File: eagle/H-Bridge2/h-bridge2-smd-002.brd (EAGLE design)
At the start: 100 x 80 mm, 29 parts

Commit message: eagle merge template board with h-br
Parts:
- RLA: device rcl:0411/15 -> rcl:R0603
- moved C4 100.6 mm to (69.8, 14.0)
- moved RLA 95.3 mm to (57.1, 15.2)
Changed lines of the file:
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@@
 </element>
 <element name="C1" library="rcl" package="C025-025X050" value="" x="55.88" y="-86.36"/>
-<element name="C4" library="rcl" package="C025-025X050" value="" x="62.23" y="-86.36"/>
+<element name="C4" library="rcl" package="C025-025X050" value="" x="69.85" y="13.97"/>
 <element name="RHA" library="rcl" package="0411/15" value="" x="20.32" y="-80.01"/>
-<element name="RLA" library="rcl" package="0411/15" value="" x="55.88" y="-80.01"/>
+<element name="RLA" library="rcl" package="R0603" value="" x="57.15" y="15.24"/>
 <element name="RHB" library="rcl" package="0411/15" value="" x="38.1" y="-80.01"/>
 <element name="RLB" library="rcl" package="0411/15" value="" x="7.62" y="-86.36"/>
@@
 <contactref element="RLA" pad="2"/>
 <contactref element="LA" pad="G"/>
-<wire x1="63.5" y1="-80.01" x2="1.27" y2="-49.53" width="0" layer="19" extent="1-1"/>
+<wire x1="58" y1="15.24" x2="1.27" y2="-49.53" width="0" layer="19" extent="1-1"/>
 </signal>
 <signal name="N$6">
@@
 <contactref element="UA" pad="1"/>
 <contactref element="RLA" pad="1"/>
-<wire x1="0" y1="-6.35" x2="48.26" y2="-80.01" width="0" layer="19" extent="1-1"/>
+<wire x1="0" y1="-6.35" x2="56.3" y2="15.24" width="0" layer="19" extent="1-1"/>
 </signal>
 <signal name="N$11">
@@
 <wire x1="39.37" y1="-86.36" x2="21.59" y2="-72.39" width="0" layer="19" extent="1-1"/>
 <wire x1="16.51" y1="-49.53" x2="21.59" y2="-72.39" width="0" layer="19" extent="1-1"/>
-<wire x1="63.5" y1="-86.36" x2="39.37" y2="-86.36" width="0" layer="19" extent="1-1"/>
-<wire x1="53.34" y1="-57.15" x2="63.5" y2="-86.36" width="0" layer="19" extent="1-1"/>
+<wire x1="71.12" y1="13.97" x2="39.37" y2="-86.36" width="0" layer="19" extent="1-1"/>
+<wire x1="53.34" y1="-57.15" x2="71.12" y2="13.97" width="0" layer="19" extent="1-1"/>
 <wire x1="19.05" y1="-16.51" x2="16.51" y2="-49.53" width="0" layer="19" extent="1-1"/>
 <wire x1="57.15" y1="-22.86" x2="53.34" y2="-57.15" width="0" layer="19" extent="1-1"/>
@@
 <contactref element="UB" pad="6"/>
 <contactref element="C4" pad="1"/>
-<wire x1="60.96" y1="-86.36" x2="0" y2="-78.74" width="0" layer="19" extent="1-1"/>
+<wire x1="68.58" y1="13.97" x2="0" y2="-78.74" width="0" layer="19" extent="1-1"/>
 <wire x1="19.05" y1="-19.05" x2="0" y2="-78.74" width="0" layer="19" extent="1-1"/>
 </signal>

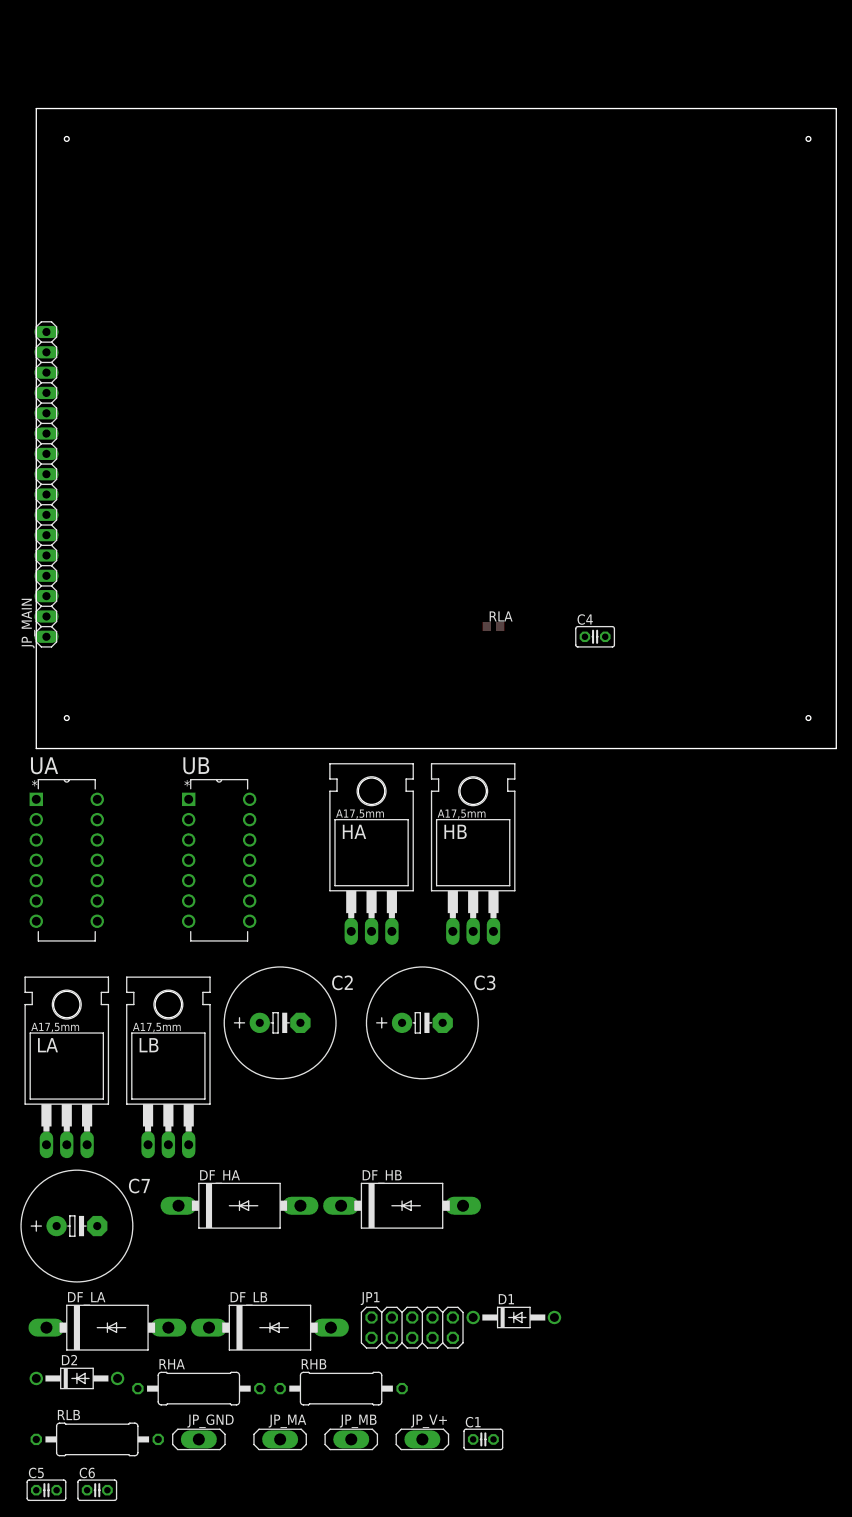
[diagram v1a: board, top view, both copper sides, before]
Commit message: H-bridge on SMD
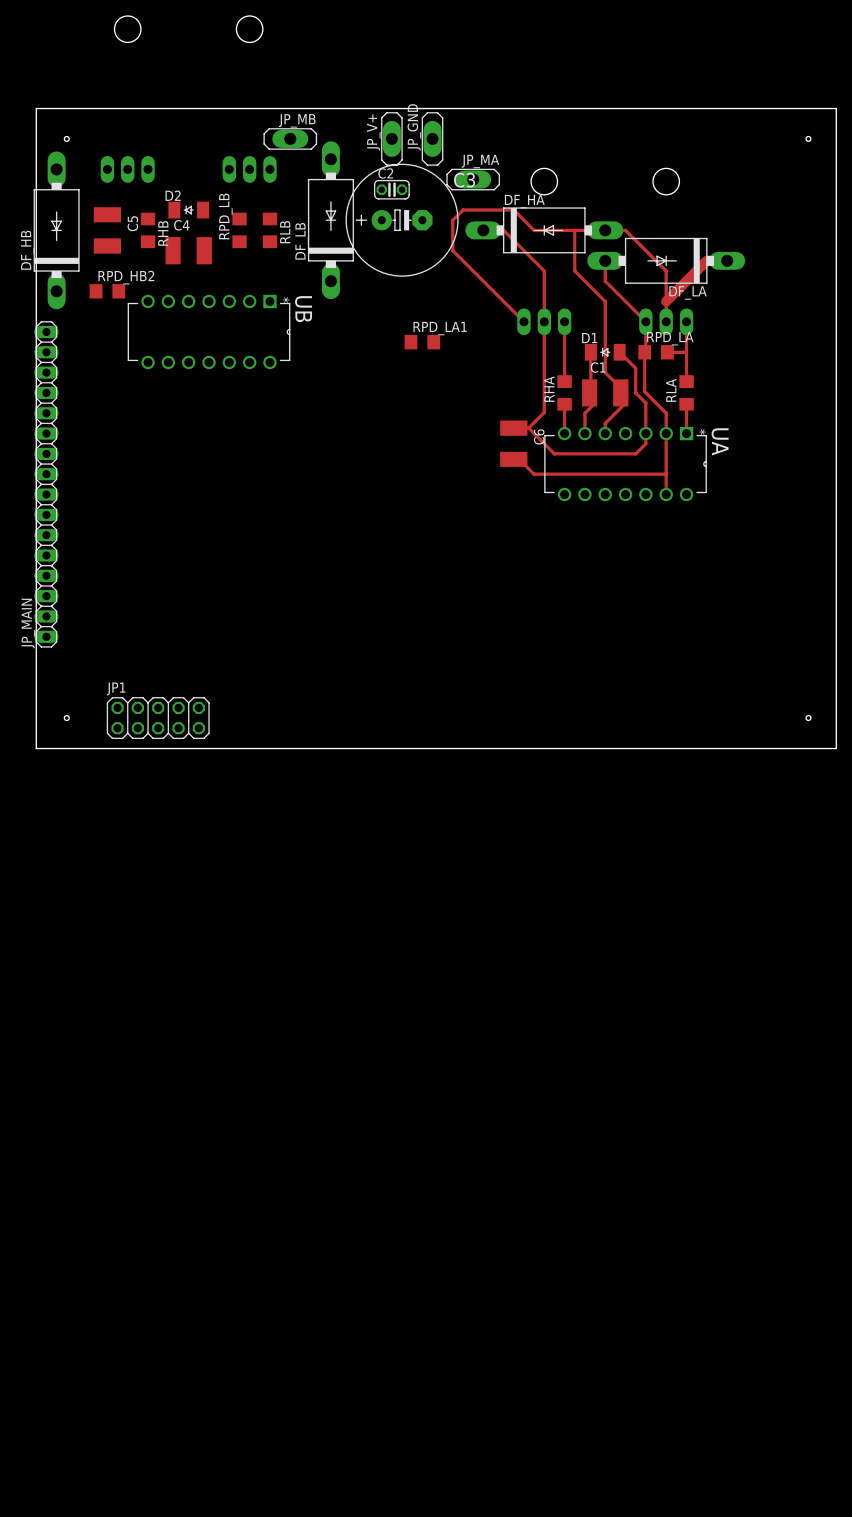
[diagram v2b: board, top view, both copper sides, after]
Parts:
- removed C7: (no value), rcl:E5-13
- added RPD_HB2, RPD_LA, RPD_LA1, RPD_LB: (no value), rcl:R1206
- C1, C4, C5, C6: device rcl:C025-025X050 -> rcl:C4532
- C2: device rcl:E5-13 -> rcl:C025-024X044
- D1, D2: value 1N4004 -> CGRM4001-G; device diode:DO41-10 -> diode:SOD-123_MINI-SMA
- RHA, RHB, RLB: device rcl:0411/15 -> rcl:R1206
- RLA: device rcl:R0603 -> rcl:R1206
- moved JP_GND 165.2 mm to (49.5, 76.2), turned to 90 degrees
- moved JP_MB 162.7 mm to (31.8, 76.2)
- moved JP_V+ 162.6 mm to (44.5, 76.2), turned to 90 degrees
- moved JP_MA 159.3 mm to (54.6, 71.1)
- moved C5 157.7 mm to (8.89, 64.8), turned to 270 degrees
- moved RLB 152.7 mm to (29.2, 64.8), turned to 270 degrees
- moved DF_LA 150.5 mm to (78.7, 61.0), turned to 180 degrees
- moved RHB 146.8 mm to (14.0, 64.8), turned to 270 degrees
- moved D2 146.7 mm to (19.1, 67.3)
- moved C6 140.8 mm to (59.7, 38.1), turned to 270 degrees
- moved DF_LB 138.6 mm to (36.8, 66.0), turned to 90 degrees
- moved RHA 132.6 mm to (66.0, 44.5), turned to 90 degrees
- moved C1 131.7 mm to (71.1, 44.5)
- moved DF_HB 129.3 mm to (2.54, 64.8), turned to 90 degrees
- moved DF_HA 127.7 mm to (63.5, 64.8)
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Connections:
- net N$13: now also C2.1; no longer C2.+, C7.+
- net N$16: now also RPD_HB2.1
- net N$17: now also RPD_LA1.1
- net N$4: now also C2.2, RPD_LA.1, RPD_LB.1; no longer C2.-, C7.-
- net N$5: now also RPD_LA.2
- net N$6: now also RPD_LA1.2
- net N$7: now also RPD_HB2.2
- net N$8: now also RPD_LB.2
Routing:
- net N$17: track 0.00 -> 92.7 mm
- net N$13: track 0.00 -> 61.3 mm
- net N$4: track 0.00 -> 52.3 mm
- net N$14: track 0.00 -> 11.0 mm
- net N$5: track 0.00 -> 9.86 mm
- net N$6: track 0.00 -> 7.47 mm
- net N$9: track 0.00 -> 3.66 mm
- net N$10: track 0.00 -> 3.66 mm

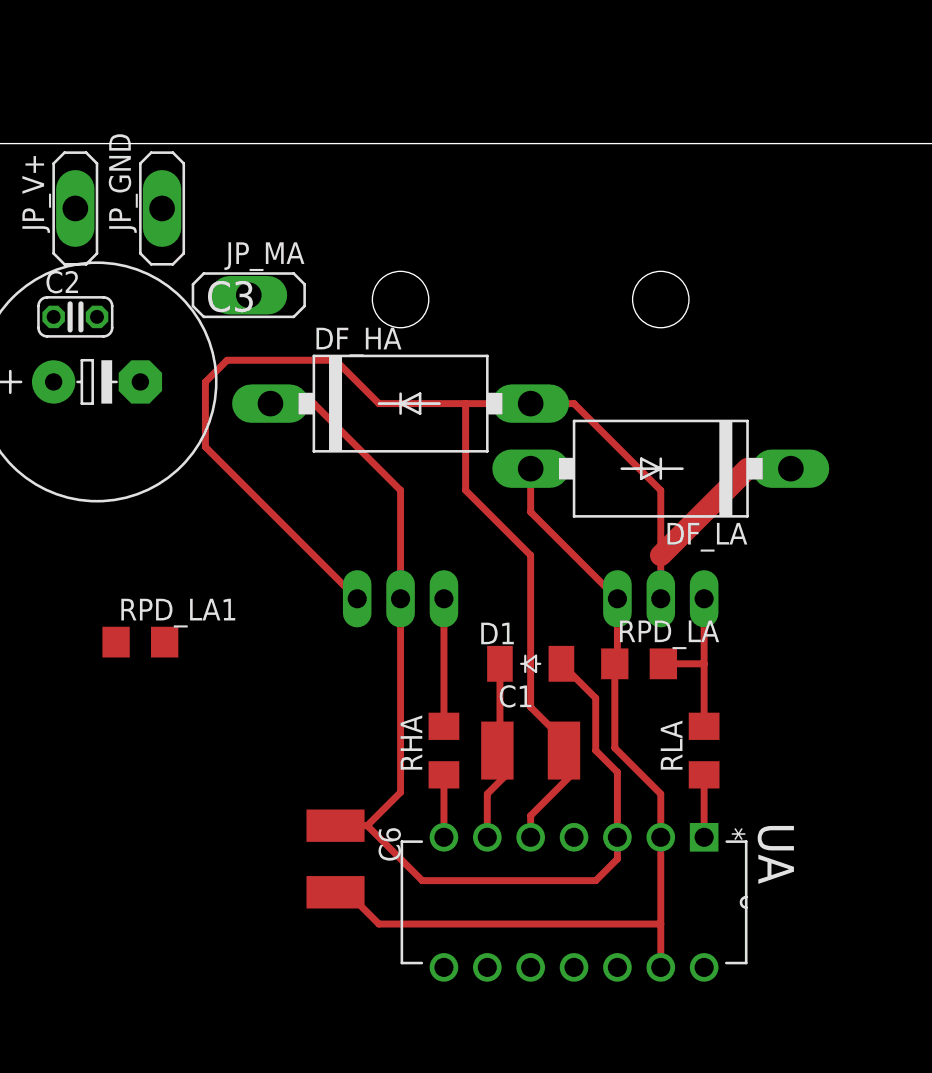
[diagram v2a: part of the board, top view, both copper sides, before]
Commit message: H-bridge smd layout
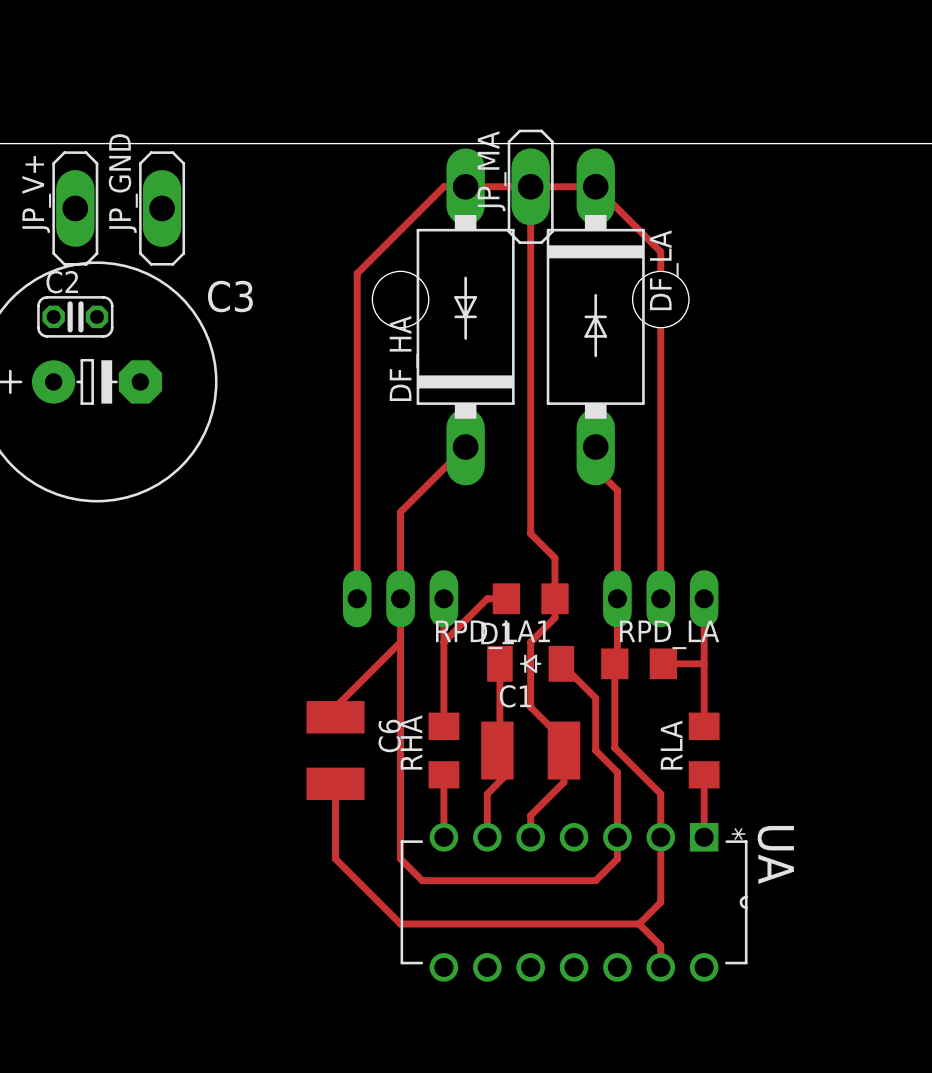
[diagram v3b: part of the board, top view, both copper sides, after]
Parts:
- moved RPD_LA1 23.0 mm to (71.1, 53.3), turned to 180 degrees
- moved JP_MA 17.7 mm to (71.1, 77.5), turned to 90 degrees
- moved DF_LA 9.67 mm to (74.9, 69.8), turned to 270 degrees
- moved C6 6.35 mm to (59.7, 44.5)
- moved DF_HA 6.35 mm to (67.3, 69.8), turned to 90 degrees
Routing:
- net N$17: track 92.7 -> 101.7 mm
- net N$4: track 52.3 -> 57.7 mm
- net N$6: track 7.47 -> 12.4 mm
- net N$13: track 61.3 -> 58.2 mm

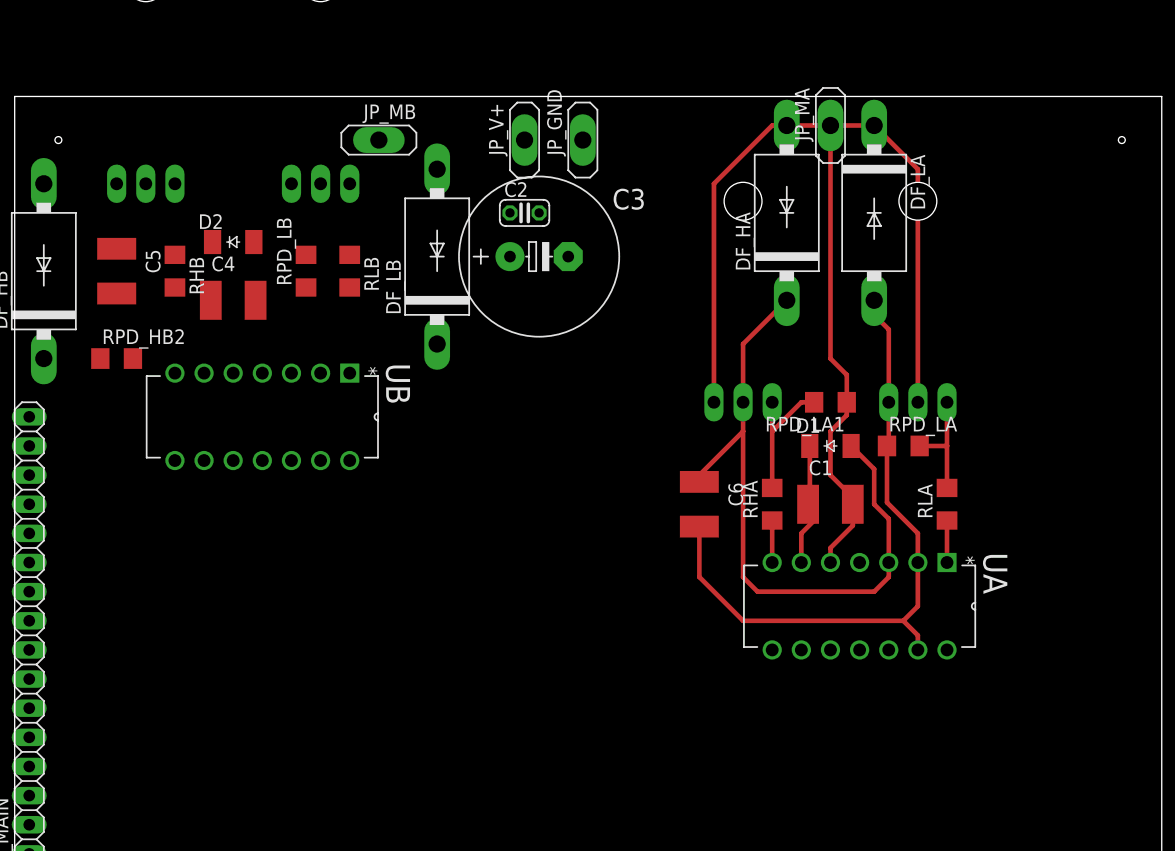
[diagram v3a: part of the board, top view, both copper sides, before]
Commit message: H-bridge smd
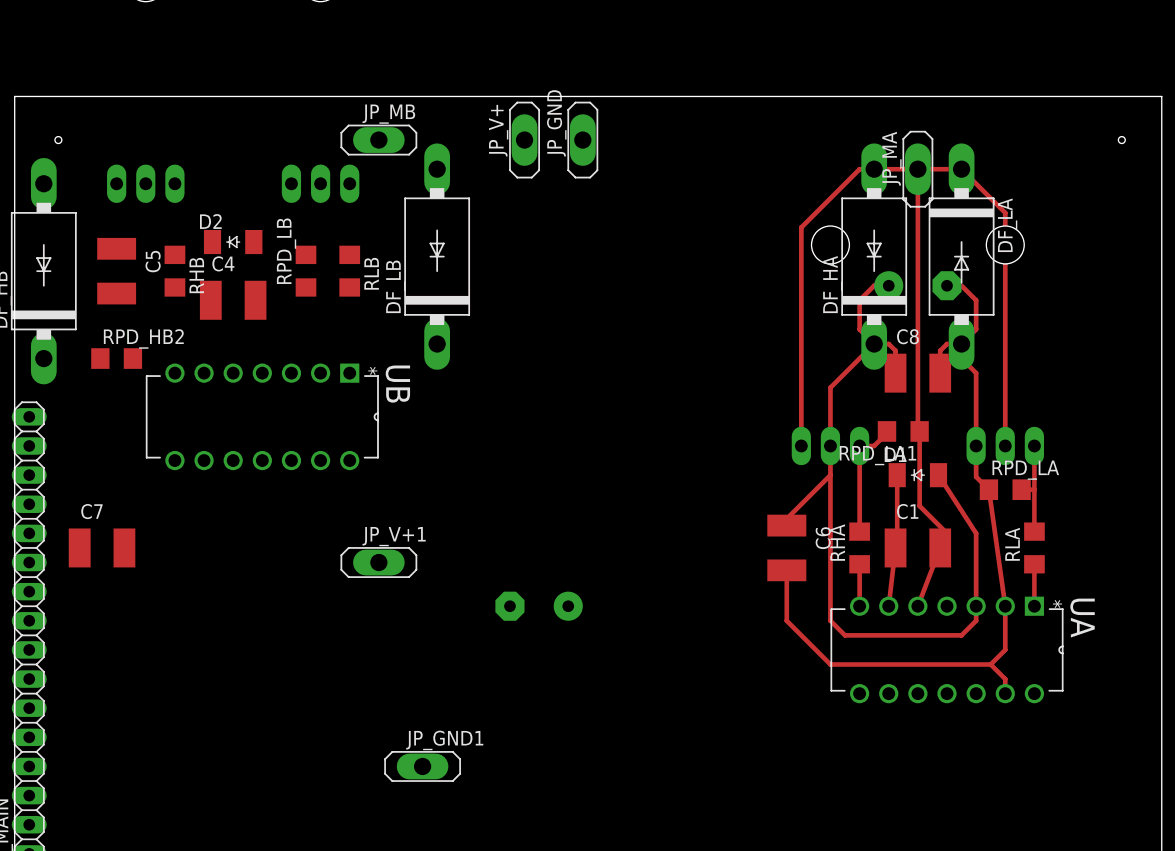
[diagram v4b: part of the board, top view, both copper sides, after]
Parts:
- removed C2: (no value), rcl:C025-024X044
- added C7, C8: (no value), rcl:C4532
- added C9: (no value), rcl:E5-13
- added JP_GND1, JP_V+1: (no value), dbg-misc:1X01
- moved C3 33.1 mm to (78.7, 63.5), flipped to the bottom, turned to 180 degrees
- moved RPD_LA 9.67 mm to (86.4, 45.7)
- moved C6 8.52 mm to (67.3, 40.6)
- moved RLA 8.52 mm to (88.9, 40.6)
- moved HA 8.52 mm to (71.1, 55.9)
- moved LA 8.52 mm to (86.4, 55.9)
- moved DF_HA 8.52 mm to (74.9, 66.0)
- moved C1 8.52 mm to (78.7, 40.6)
- moved JP_MA 8.52 mm to (78.7, 73.7)
- moved RHA 8.52 mm to (73.7, 40.6)
- moved UA 8.52 mm to (73.7, 27.9)
- moved DF_LA 8.52 mm to (82.5, 66.0)
- moved D1 8.03 mm to (78.7, 47.0)
- moved RPD_LA1 6.84 mm to (77.5, 50.8)
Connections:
- net N$13: now also C7.1, C8.1, C9.+, JP_V+1.1; no longer C2.1
- net N$4: now also C7.2, C8.2, C9.-, JP_GND1.1; no longer C2.2
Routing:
- net N$13: track 58.2 -> 71.1 mm
- net N$4: track 57.7 -> 67.5 mm
- net N$14: track 11.0 -> 13.1 mm
- net N$6: track 12.4 -> 10.5 mm
- net N$5: track 9.86 -> 8.59 mm
- net N$17: track 101.7 -> 100.6 mm
